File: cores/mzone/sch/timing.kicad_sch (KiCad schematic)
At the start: 34 parts

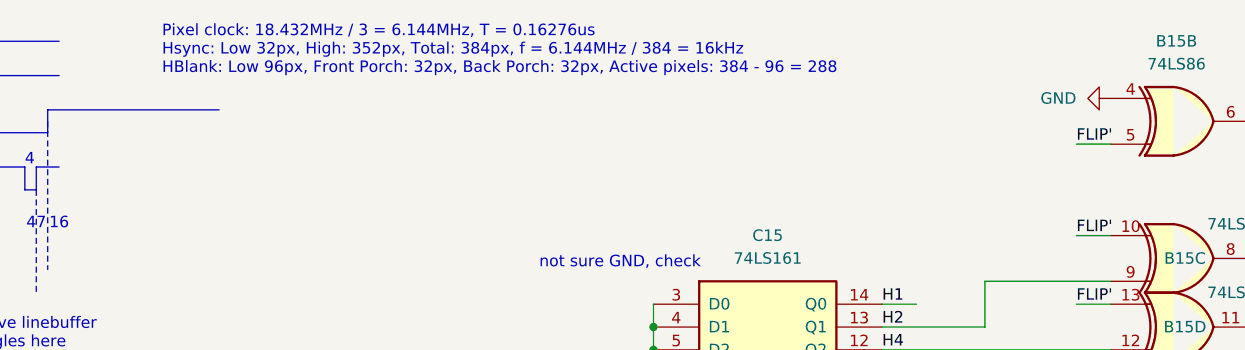
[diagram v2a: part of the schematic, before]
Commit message: mzone core
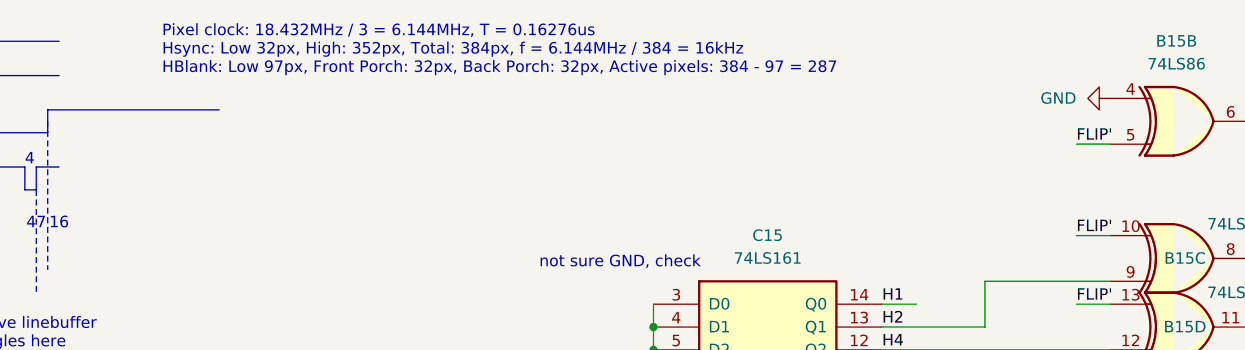
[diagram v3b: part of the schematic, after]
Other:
- note added: "Pixel clock: 18.432MHz / 3 = 6.144MHz, T = 0.16276us Hsync: Low 32px, High: 352px, Total: 384px, f = 6.144MHz / 384 = 16kHz HBlank: Low 97px, Front Porch: 32px, Back Porch: 32px, Active pixels: 384 - 97 = 287"
- note removed: "Pixel clock: 18.432MHz / 3 = 6.144MHz, T = 0.16276us Hsync: Low 32px, High: 352px, Total: 384px, f = 6.144MHz / 384 = 16kHz HBlank: Low 96px, Front Porch: 32px, Back Porch: 32px, Active pixels: 384 - 96 = 288"
